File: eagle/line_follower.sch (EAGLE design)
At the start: 44 parts, among them IC1 A4950, IC2 A4950, IC3 7805DT, IC4 LM317LD, J1 XT-60NO_LABEL, J2 22-27-2031-03, SW1 12MM_BUTTON, U1 TEENSY_3.1_BASIC, U2 MPU6050_BREAKOUT, X1 1.5MM_PAD, X2 1.5MM_PAD, X3 1.5MM_PAD, X4 1.5MM_PAD

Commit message: Fixes before sending the board for fab.
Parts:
- removed U$1: LINE_FOLLOWER_HEATSINK, untitled:LINE_FOLLOWER_HEATSINK
- removed U1: TEENSY_3.1_BASIC, Teensy_3_Series_Board_v1.0:TEENSY_3.1_BASIC
- removed U2: MPU6050_BREAKOUT, untitled:MPU6050_BREAKOUT
- added M1B, M2A: 1.5MM_PAD, untitled:1.5MM_PAD
- C2, C3: value 100nF -> 100uF 16V; device rcl:C-EUC0805 -> rcl:CPOL-EUUD-6,3X8,8
- C4, C6: value 100uF 16V -> 100nF; device rcl:CPOL-EUUD-6,3X8,8 -> rcl:C-EUC0805
- Q1, Q2, Q3, Q4: device SparkFun-DiscreteSemi:PHOTOTRANSISTORPT17-21C-L41-TR8 -> untitled:PHOTOTRANSISTOR1206
- R6, R7: value 0R15 -> 1R 1% 0.125W; device rcl:R-EU_R2512 -> rcl:R-EU_R0805
- R8: value 470 -> 4k7
- R9: value 470 -> 1k5
- X1: value 1.5MM_PAD -> TEENSY_3.1_BASIC; device untitled:1.5MM_PAD -> Teensy_3_Series_Board_v1.0:TEENSY_3.1_BASIC
- X2: value 1.5MM_PAD -> MPU6050_BREAKOUT; device untitled:1.5MM_PAD -> untitled:MPU6050_BREAKOUT
- renumbered C5 to C7, X3 to M1A, X4 to M2B
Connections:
- net +3V3: now also Q1.C, Q2.C, Q3.C, Q4.C, X1.3.3V; no longer IC1.VREF, IC2.VREF, U1.3.3V
- net +5V: now also C4.1, IC1.VREF, IC2.VREF, X1.VIN, X2.VCC; no longer C2.1, Q1.C, Q2.C, Q3.C, Q4.C, U1.VIN, U2.VCC
- net BUTTON: now also X1.12/MISO; no longer U1.12/MISO
- net GND: now also C2.-, C3.-, C4.2, C6.2, X1.AGND, X1.GND, X2.GND; no longer C2.2, C3.2, C4.-, C6.-, U$1.P$1, U1.AGND, U1.GND, U2.GND
- net I_SENSE0: now also X1.21/A7/PWM; no longer U1.21/A7/PWM
- net I_SENSE1: now also X1.20/A6/PWM; no longer U1.20/A6/PWM
- net LINE0: now also X1.17/A3/T; no longer U1.17/A3/T
- net LINE1: now also X1.16/A2/T; no longer U1.16/A2/T
- net LINE2: now also X1.15/A1/T; no longer U1.15/A1/T
- net LINE3: now also X1.14/A0; no longer U1.14/A0
- net LINE_LED0: now also X1.7/RX3; no longer U1.7/RX3
- net LINE_LED1: now also X1.8/TX3; no longer U1.8/TX3
- net LINE_LED2: now also X1.9/RX2/PWM; no longer U1.9/RX2/PWM
- net LINE_LED3: now also X1.10/TX2/PWM; no longer U1.10/TX2/PWM
- net LINE_LED4: now also X1.11/MOSI; no longer U1.11/MOSI
- net MOTOR0A: now also X1.3/CAN-TX/PWM; no longer U1.3/CAN-TX/PWM
- net MOTOR0B: now also X1.4/CAN-RX-PWM; no longer U1.4/CAN-RX-PWM
- net MOTOR1A: now also X1.5/PWM; no longer U1.5/PWM
- net MOTOR1B: now also X1.6/PWM; no longer U1.6/PWM
- net N$3: now also M2A.P$1; no longer X2.P$1
- net N$4: now also M1B.P$1; no longer X1.P$1
- net N$5: now also C3.+; no longer C1.+
- net RANGE: now also X1.23/A9/T/PWM; no longer U1.23/A9/T/PWM
- net SCL: now also X1.19/A5/T/SCL0, X2.SCL; no longer U1.19/A5/T/SCL0, U2.SCL
- net SDA: now also X1.18/A4/T/SDA0, X2.SDA; no longer U1.18/A4/T/SDA0, U2.SDA
- net U_SENSE: now also X1.22/A8/T/PWM; no longer U1.22/A8/T/PWM
- net VCC: now also C1.+, C2.+, C6.1; no longer C3.1, C4.+, C6.+
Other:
- moved on the sheet: C1

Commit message: Fixed values of line sensor divider resistors.
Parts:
- R1, R2, R3, R4: value 470 -> 10k
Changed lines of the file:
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@@
 <?xml version="1.0" encoding="utf-8"?>
 <!DOCTYPE eagle SYSTEM "eagle.dtd">
-<eagle version="7.4.0">
+<eagle version="7.7.0">
 <drawing>
 <settings>
@@
 <part name="LED5" library="led" deviceset="LED" device="CHIPLED_0603"/>
 <part name="R5" library="rcl" deviceset="R-EU_" device="R0805" value="68"/>
-<part name="R1" library="rcl" deviceset="R-EU_" device="R0805" value="470"/>
-<part name="R2" library="rcl" deviceset="R-EU_" device="R0805" value="470"/>
-<part name="R3" library="rcl" deviceset="R-EU_" device="R0805" value="470"/>
-<part name="R4" library="rcl" deviceset="R-EU_" device="R0805" value="470"/>
+<part name="R1" library="rcl" deviceset="R-EU_" device="R0805" value="10k"/>
+<part name="R2" library="rcl" deviceset="R-EU_" device="R0805" value="10k"/>
+<part name="R3" library="rcl" deviceset="R-EU_" device="R0805" value="10k"/>
+<part name="R4" library="rcl" deviceset="R-EU_" device="R0805" value="10k"/>
 <part name="GND10" library="supply1" deviceset="GND" device=""/>
 <part name="M1B" library="untitled" deviceset="1.5MM_PAD" device=""/>

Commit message: Schematic for V2 mostly complete, time to work on the board.
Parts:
- removed IC4: LM317LD, linear:LM317LD
- removed LED10, LED7, LED8, LED9: (no value), led:LEDSML0805
- removed M1A, M1B, M2A, M2B: 1.5MM_PAD, untitled:1.5MM_PAD
- removed R6, R7: 1R 1% 0.125W, rcl:R-EU_R0805
- removed R8: 4k7, rcl:R-EU_R0805
- added C10, C11, C12, C8, C9: 100n, rcl:C-EUC0805
- added C5: 100nF, rcl:C-EUC0805
- added J3, J4: 22-27-2061-06, con-molex:22-27-2061-06
- added Q5: ALS-PT19-315C/L177/TR8, untitled:ALS-PT19-315C/L177/TR8
- added R10: 1k5, rcl:R-EU_R0805
- C1, C2, C3: value 100uF 16V -> 100uF 25V
- IC3: value 7805DT -> MC78M05 (??)
- J1: value XT-60NO_LABEL -> 2S - 4S LiPo
- LED1, LED2, LED3, LED4, LED5: value (none) -> APT2012EC; device led:LEDCHIPLED_0603 -> led:LEDCHIP-LED0805
- LED6: value (none) -> APT2012EC; device led:LEDSML0805 -> led:LEDCHIP-LED0805
- Q1, Q2, Q3, Q4: value (none) -> ALS-PT19-315C/L177/TR8; device untitled:PHOTOTRANSISTOR1206 -> untitled:ALS-PT19-315C/L177/TR8
- R1, R2, R3, R4: value 10k -> 5k6
- R5: value 68 -> 5k6
- R9: value 1k5 -> 4k7
- X1: value TEENSY_3.1_BASIC -> ESP32DEVKITV1; device Teensy_3_Series_Board_v1.0:TEENSY_3.1_BASIC -> ESP32-DEVKITV1:ESP32DEVKITV1
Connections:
- removed net I_SENSE0: IC1.LSS, R6.1, X1.21/A7/PWM
- removed net I_SENSE1: IC2.LSS, R7.1, X1.20/A6/PWM
- removed net LINE0: Q1.E, R1.1, X1.17/A3/T
- removed net LINE1: Q2.E, R2.1, X1.16/A2/T
- removed net LINE2: Q3.E, R3.1, X1.15/A1/T
- removed net LINE3: Q4.E, R4.1, X1.14/A0
- removed net LINE_LED3: LED4.C, X1.10/TX2/PWM
- removed net LINE_LED4: LED5.C, X1.11/MOSI
- removed net N$10: LED4.A, LED9.C
- removed net N$11: IC4.ADJ, LED10.A, LED6.A, LED7.A, LED8.A, LED9.A, R5.2
- removed net N$12: LED10.C, LED5.A
- removed net N$14: IC4.VO, IC4.VO@1, IC4.VO@2, IC4.VO@3, R5.1
- removed net N$5: C3.+, D1.C, IC3.VI
- removed net N$8: LED3.A, LED8.C
- removed net U_SENSE: R8.2, R9.1, X1.22/A8/T/PWM
- new net BAT_SENSE: R10.1, R9.2, X1.IO14
- new net ENCODER0A: J3-3.S, X1.IO5
- new net ENCODER0B: J3-4.S, X1.IO17
- new net ENCODER1A: J4-4.S, X1.IO2
- new net ENCODER1B: J4-3.S, X1.IO15
- new net LINE_SENSOR0: C8.2, Q1.E, R1.2, X1.IO32
- new net LINE_SENSOR1: C9.2, Q2.E, R2.2, X1.IO13
- new net LINE_SENSOR2: C10.2, Q3.E, R3.2, X1.IO33
- new net LINE_SENSOR3: C11.2, Q4.E, R4.2, X1.IO12
- new net LINE_SENSOR4: C12.2, Q5.E, R5.2, X1.IO34
- new net MPU6050_INT: X1.IO1, X2.INT
- net +3V3: now also IC1.VREF, IC2.VREF, J3-2.S, J4-2.S, Q5.C, X1.3V3; no longer X1.3.3V
- net +5V: now also C1.+, D1.C; no longer C4.1, IC1.VREF, IC2.VREF, IC3.VO, IC4.VI
- net BUTTON: now also X1.IO3; no longer X1.12/MISO
- net GND: now also C10.1, C11.1, C12.1, C5.2, C8.1, C9.1, IC1.LSS, IC2.LSS, J3-5.S, J4-5.S, R1.1, R10.2, R2.1, R3.1, R4.1, R5.1, X1.GND1; no longer R1.2, R2.2, R3.2, R4.2, R6.2, R7.2, R9.2, X1.AGND
- net LINE_LED0: now also LED2.A, LED5.C, LED6.A, X1.IO27; no longer X1.7/RX3
- net LINE_LED1: now also LED1.A, LED3.C, LED4.A, X1.IO26; no longer X1.8/TX3
- net LINE_LED2: now also LED3.A, LED4.C, LED5.A, LED6.C, X1.IO25; no longer LED3.C, X1.9/RX2/PWM
- net MOTOR0A: now also IC1.IN1, X1.IO19; no longer IC1.IN2, X1.3/CAN-TX/PWM
- net MOTOR0B: now also IC1.IN2, X1.IO18; no longer IC1.IN1, X1.4/CAN-RX-PWM
- net MOTOR1A: now also X1.IO16; no longer X1.5/PWM
- net MOTOR1B: now also X1.IO4; no longer X1.6/PWM
- net N$1: now also J3-1.S; no longer M1A.P$1
- net N$2: now also IC2.OUT1, J4-1.S; no longer IC2.OUT2, M2B.P$1
- net N$3: now also IC2.OUT2, J4-6.S; no longer IC2.OUT1, M2A.P$1
- net N$4: now also J3-6.S; no longer M1B.P$1
- net N$6: now also C7.1, D1.A, IC3.VO; no longer LED1.A, LED6.C
- net N$7: now also C4.1, IC3.VI; no longer LED2.A, LED7.C
- net RANGE: now also X1.IO35; no longer X1.23/A9/T/PWM
- net SCL: now also X1.IO22; no longer X1.19/A5/T/SCL0
- net SDA: now also X1.IO21; no longer X1.18/A4/T/SDA0
- net VCC: now also C3.+, C5.1, R9.1; no longer C1.+, C7.1, D1.A, R8.1
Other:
- note added: "Line sensor LEDs Charlieplexing leds, using ESP32 GPIO drive strength to limit current. Should be fairly safe even at max drive strength at about 30mA per LED. See https://www.esp32.com/viewtopic.php?f=12&t=5840#p25550"
- note added: "Power supply Both ESP32-DEVKITV1 and GY-521 have on board 3.3V regulators. We're using the one on ESP32 to power small stuff around the board."
- note removed: "18.3mA"
- note removed: "3S LiPo -- 12.6 V max, 11.1 V nominal, 10.5 V min"
- note removed: "IR leds (bottom)"
- note removed: "Indicator LEDs (top)"
- note removed: "Power supply"
- moved on the sheet: C1, C2, C3, C4, C6, C7, D1, IC1, IC2, IC3, J1, LED1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

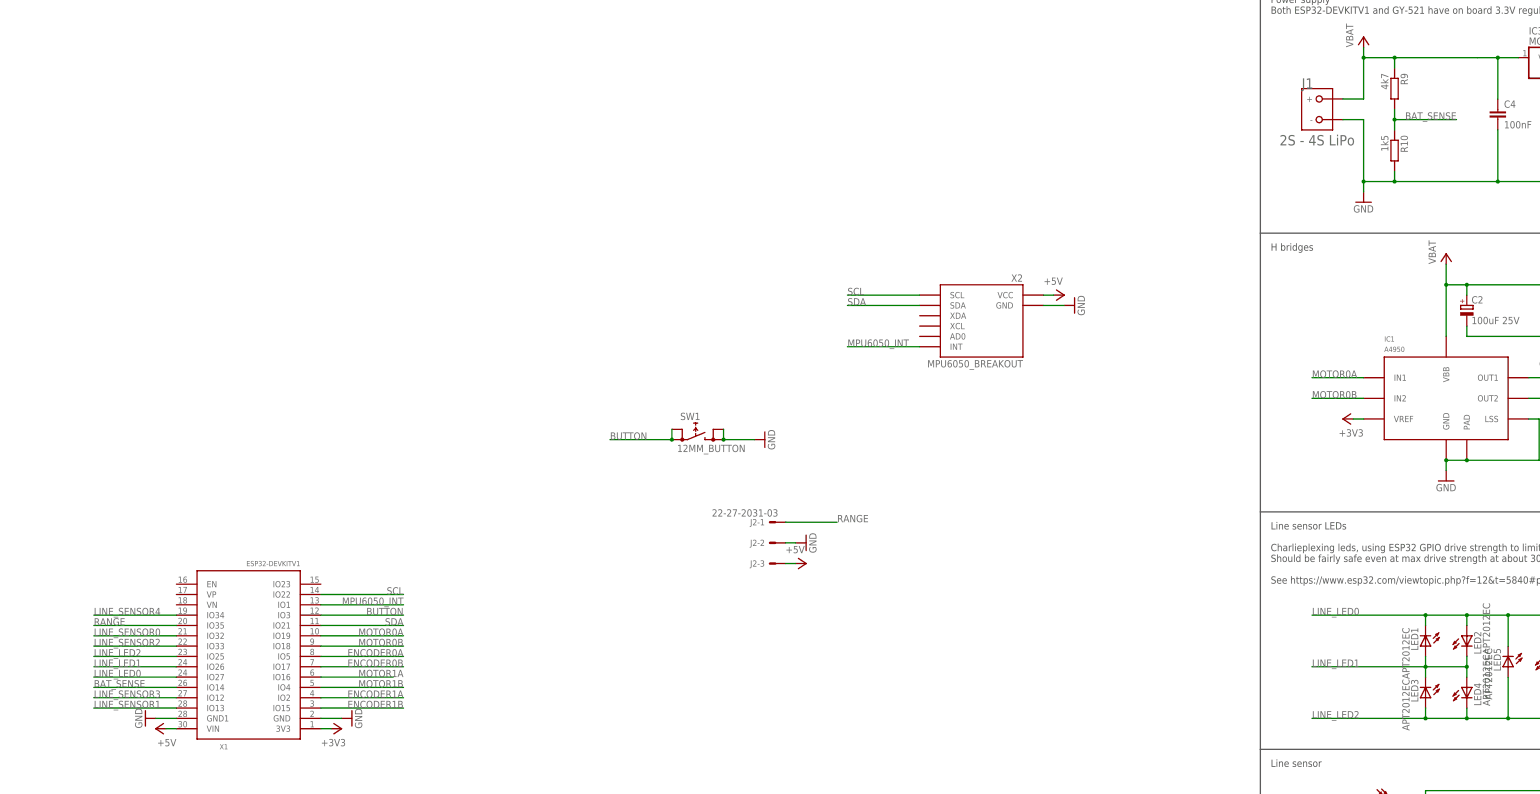
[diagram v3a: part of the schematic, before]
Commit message: Updated gitignore
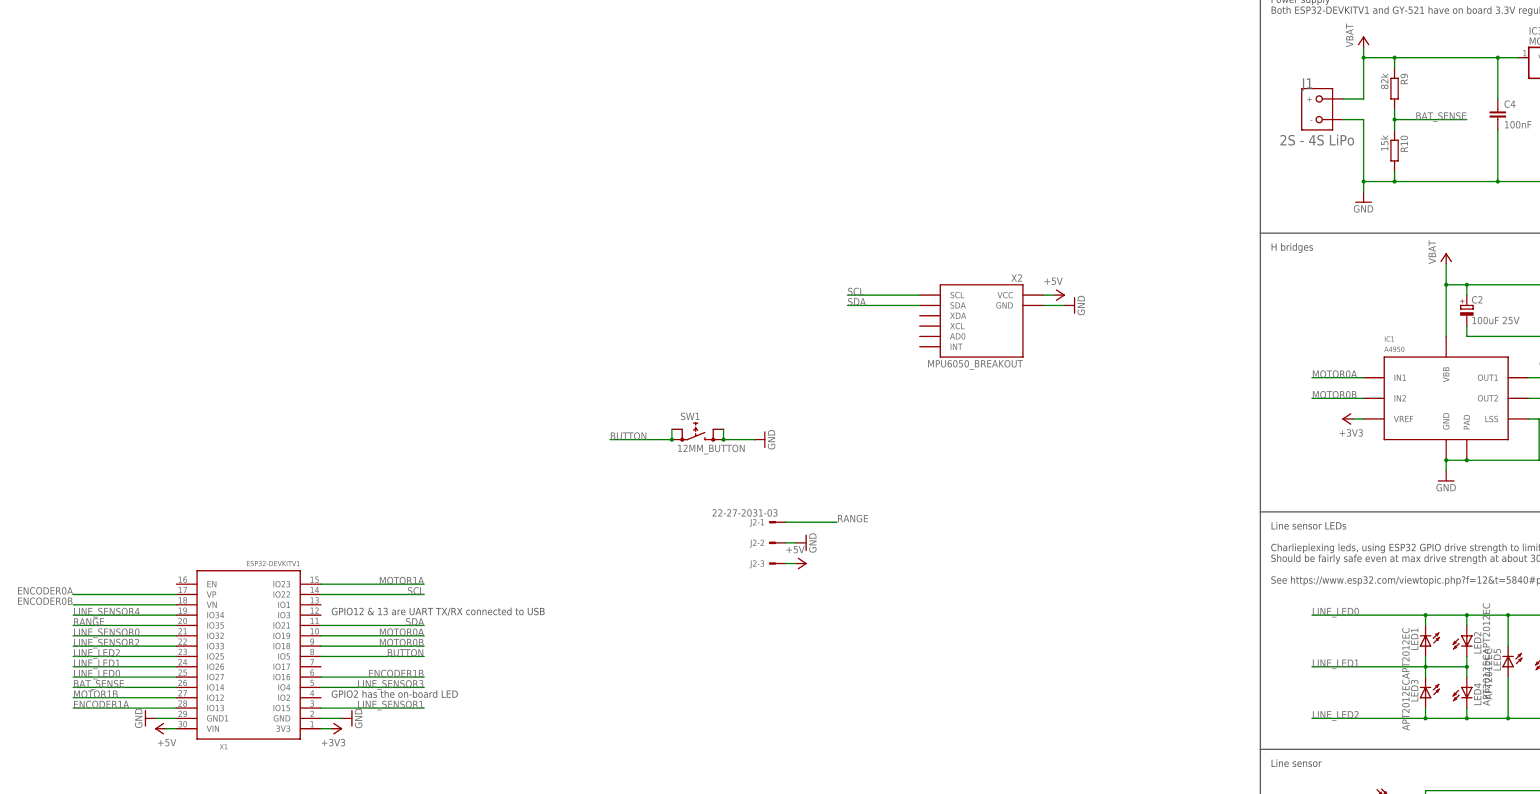
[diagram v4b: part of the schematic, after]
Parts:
- R10: value 1k5 -> 15k
- R9: value 4k7 -> 82k
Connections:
- removed net MPU6050_INT: X1.IO1, X2.INT
- net BUTTON: now also X1.IO5; no longer X1.IO3
- net ENCODER0A: no longer X1.IO5
- net ENCODER0B: no longer X1.IO17
- net ENCODER1A: now also X1.IO13; no longer X1.IO2
- net ENCODER1B: now also X1.IO16; no longer X1.IO15
- net LINE_SENSOR1: now also X1.IO15; no longer X1.IO13
- net LINE_SENSOR3: now also X1.IO4; no longer X1.IO12
- net MOTOR1A: no longer X1.IO16
- net MOTOR1B: now also X1.IO12; no longer X1.IO4
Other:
- note added: "GPIO12 & 13 are UART TX/RX connected to USB"
- note added: "GPIO2 has the on-board LED"

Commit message: Decided to not use the encoder board on the motors, schematic tweaks and start of layout
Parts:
- removed D1: (no value), diode:DIODE-MELF-MLL41
- removed J3, J4: 22-27-2061-06, con-molex:22-27-2061-06
- removed R10: 15k, rcl:R-EU_R0805
- removed R9: 82k, rcl:R-EU_R0805
- added C13: 100nF, rcl:C-EUC0805
- added M1, M2: N20-ENC, untitled:N20-ENC
- added R6, R7: 5k6, rcl:R-EU_R0805
- added U$1, U$2: SI7202, untitled:SI7202
- C12: value 100n -> 100nF
- C2: value 100uF 25V -> 100nF; device rcl:CPOL-EUUD-6,3X8,8 -> rcl:C-EUC0805
- C6: value 100nF -> 22uF
- C7: value 100nF -> 100n
- IC3: value MC78M05 (??) -> NCV4274CDT50RKG
- J1: value 2S - 4S LiPo -> XT60PW-M; device RoboJackets-Connectors:XT-60NO_LABEL -> untitled:XT60PW-M
- R1: value 5k6 -> 15k
- R2: value 5k6 -> 82k
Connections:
- removed net ENCODER0A: J3-3.S
- removed net ENCODER0B: J3-4.S
- removed net ENCODER1A: J4-4.S, X1.IO13
- removed net ENCODER1B: J4-3.S, X1.IO16
- removed net N$6: C7.1, D1.A, IC3.VO
- removed net N$7: C4.1, IC3.VI
- removed net VCC: C2.+, C3.+, C5.1, C6.1, IC1.VBB, IC2.VBB, J1.+, R9.1
- new net ENCODER0: U$2.OUT, X1.IO17
- new net ENCODER1: U$1.OUT, X1.IO16
- new net VBAT: C1.+, C2.1, C3.+, C4.1, C5.1, IC1.VBB, IC2.VBB, IC3.VI, J1.+, R2.1
- net +3V3: now also C12.1, C13.1, U$1.VDD, U$2.VDD; no longer J3-2.S, J4-2.S
- net +5V: now also C6.1, IC3.VO; no longer C1.+, D1.C
- net BAT_SENSE: now also R1.1, R2.2; no longer R10.1, R9.2
- net GND: now also C12.2, C13.2, C2.2, C7.1, R1.2, R6.1, R7.1, U$1.GND, U$2.GND; no longer C12.1, C2.-, C7.2, J3-5.S, J4-5.S, R1.1, R10.2, R2.1
- net LINE_SENSOR0: now also C7.2, R3.2; no longer C8.2, R1.2
- net LINE_SENSOR1: now also C8.2, R4.2; no longer C9.2, R2.2
- net LINE_SENSOR2: now also C9.2, R5.2; no longer C10.2, R3.2
- net LINE_SENSOR3: now also C10.2, R6.2; no longer C11.2, R4.2
- net LINE_SENSOR4: now also C11.2, R7.2; no longer C12.2, R5.2
- net MOTOR1A: now also X1.IO23
- net N$1: now also M1.P$2; no longer J3-1.S
- net N$2: now also M2.P$2; no longer J4-1.S
- net N$3: now also M2.P$1; no longer J4-6.S
- net N$4: now also M1.P$1; no longer J3-6.S
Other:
- note added: "Encoders"
- note added: "GPIO1 & 3 are UART TX/RX connected to USB"
- note removed: "GPIO12 & 13 are UART TX/RX connected to USB"
- moved on the sheet: C1, C10, C11, C12, C4, C5, C6, C7, C8, C9, LED1, LED2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

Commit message: Motor encoder boards are back, more layout work
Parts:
- removed C12, C13: 100nF, rcl:C-EUC0805
- removed SW1: 12MM_BUTTON, untitled:12MM_BUTTON
- removed U$1, U$2: SI7202, untitled:SI7202
- added S1: TACTILE-SWITCH, cube:TACTILE-SWITCH
- J2: value 22-27-2031-03 -> 2.54MM_HEADER_3X1; device con-molex:22-27-2031-03 -> untitled:2.54MM_HEADER_3X1
- M1, M2: value N20-ENC -> N20-ENC2; device untitled:N20-ENC -> untitled:N20-ENC2
- renumbered IC3 to IC5
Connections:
- removed net ENCODER0: U$2.OUT, X1.IO17
- removed net ENCODER1: U$1.OUT, X1.IO16
- new net ACCEL_INT: X1.IO18, X2.INT
- new net ENCODER0A: M1.A, X1.IO17
- new net ENCODER0B: M1.B, X1.IO16
- new net ENCODER1A: M2.B, X1.VP
- new net ENCODER1B: M2.A, X1.VN
- net +3V3: now also M1.VCC, M2.VCC; no longer C12.1, C13.1, U$1.VDD, U$2.VDD
- net +5V: now also J2.3; no longer J2-3.S
- net BAT_SENSE: now also X1.IO15; no longer X1.IO14
- net BUTTON: now also S1.A0, S1.B0; no longer SW1.A, SW1.A1
- net GND: now also J2.2, M1.GND, M2.GND, S1.A1, S1.B1; no longer C12.2, C13.2, J2-2.S, SW1.B, SW1.B1, U$1.GND, U$2.GND
- net LINE_SENSOR0: now also X1.IO33; no longer X1.IO32
- net LINE_SENSOR1: now also X1.IO14; no longer X1.IO15
- net LINE_SENSOR2: now also X1.IO32; no longer X1.IO33
- net MOTOR0A: now also X1.IO12; no longer X1.IO19
- net MOTOR0B: now also X1.IO13; no longer X1.IO18
- net MOTOR1A: now also X1.IO19; no longer X1.IO23
- net MOTOR1B: now also X1.IO23; no longer X1.IO12
- net N$1: now also M1.M+; no longer M1.P$2
- net N$2: now also M2.M+; no longer M2.P$2
- net N$3: now also M2.M-; no longer M2.P$1
- net N$4: now also M1.M-; no longer M1.P$1
- net RANGE: now also J2.1; no longer J2-1.S
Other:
- note removed: "Encoders"
- moved on the sheet: C10, C11, C3, C4, C7, C8, C9, IC2, LED1, LED2, LED3, LED4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

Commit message: Another quarter-afternoon of layout
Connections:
- net ENCODER1A: now also X1.VN; no longer X1.VP
- net ENCODER1B: now also X1.VP; no longer X1.VN
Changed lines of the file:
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@@
 </segment>
 <segment>
-<pinref part="X1" gate="G$1" pin="VN"/>
-<wire x1="-271.78" y1="-22.86" x2="-297.18" y2="-22.86" width="0.1524" layer="91"/>
-<label x="-297.18" y="-22.86" size="1.778" layer="95"/>
+<pinref part="X1" gate="G$1" pin="VP"/>
+<wire x1="-271.78" y1="-20.32" x2="-297.18" y2="-20.32" width="0.1524" layer="91"/>
+<label x="-297.18" y="-20.32" size="1.778" layer="95"/>
 </segment>
 </net>
@@
 </segment>
 <segment>
-<pinref part="X1" gate="G$1" pin="VP"/>
-<wire x1="-271.78" y1="-20.32" x2="-297.18" y2="-20.32" width="0.1524" layer="91"/>
-<label x="-297.18" y="-20.32" size="1.778" layer="95"/>
+<pinref part="X1" gate="G$1" pin="VN"/>
+<wire x1="-271.78" y1="-22.86" x2="-297.18" y2="-22.86" width="0.1524" layer="91"/>
+<label x="-297.18" y="-22.86" size="1.778" layer="95"/>
 </segment>
 </net>

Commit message: Everything is connected on the board, but more work remains
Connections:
- net +3V3: no longer IC1.VREF, IC2.VREF
- net +5V: now also IC1.VREF, IC2.VREF
- net LINE_LED0: now also LED1.A, LED2.C, LED5.A, LED6.C, X1.IO25; no longer LED1.C, LED2.A, LED5.C, LED6.A, X1.IO27
- net LINE_LED1: now also LED3.A, LED4.C, LED5.C, LED6.A; no longer LED1.A, LED2.C, LED3.C, LED4.A
- net LINE_LED2: now also LED1.C, LED2.A, LED3.C, LED4.A, X1.IO27; no longer LED3.A, LED4.C, LED5.A, LED6.C, X1.IO25
- net LINE_SENSOR0: now also X1.IO34; no longer X1.IO33
- net LINE_SENSOR1: now also X1.IO4; no longer X1.IO14
- net LINE_SENSOR3: now also X1.IO14; no longer X1.IO4
- net LINE_SENSOR4: now also X1.IO33; no longer X1.IO34
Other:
- note added: "H bridge We are not using current limiting, 5V is just tied to vref because it was close for routing"
- note removed: "H bridges"
- moved on the sheet: C1, C10, C11, C2, C3, C4, C7, C8, C9, IC1, IC2, LED1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
